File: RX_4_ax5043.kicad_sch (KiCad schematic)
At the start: 17 parts, among them U505 AX5043, U506 TPS22929D

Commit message: Add a CPU thermsistor
Signed-off-by: Corey Minyard <corey@minyard.net>
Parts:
- C550: footprint Capacitor_SMD:C_0402_1005Metric -> Capacitor_SMD:C_0603_1608Metric_Pad1.08x0.95mm_HandSolder
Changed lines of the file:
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@@
 			)
 		)
-		(property "Footprint" "Capacitor_SMD:C_0402_1005Metric"
+		(property "Footprint" "Capacitor_SMD:C_0603_1608Metric_Pad1.08x0.95mm_HandSolder"
 			(at 300.6852 85.09 0)
 			(effects

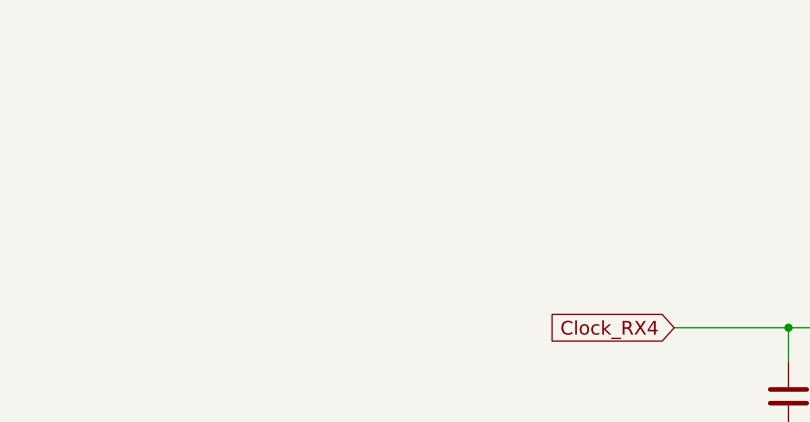
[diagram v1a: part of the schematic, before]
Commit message: Add shields around AX5043s, replace UFL connectors
Signed-off-by: Corey Minyard <corey@minyard.net>
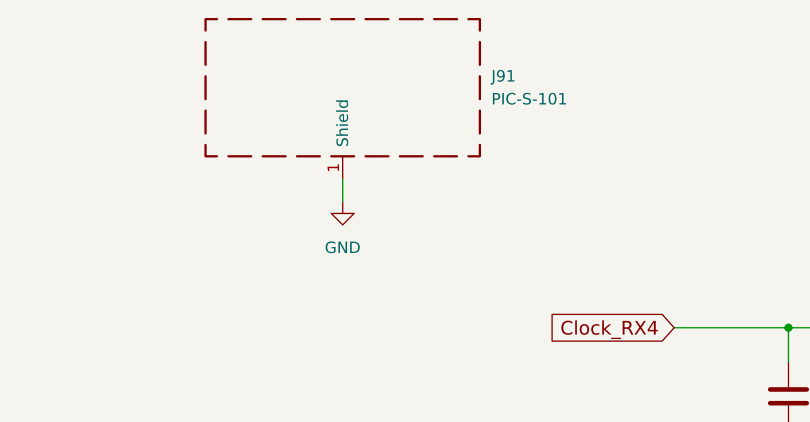
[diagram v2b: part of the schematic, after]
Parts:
- added J91: PIC-S-101, PacSatDev_misc:RF_SHIELD_PIC_S_101, symbol Device:RFShield_OnePiece
- P501: value ~ -> CONUFL001-SMD-T; footprint PacSatDev_misc:U_FL -> PacSatDev_misc:CONN1_CONUFL_TEC
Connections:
- net GND: now also J91.1 (Shield)
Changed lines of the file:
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@@
+	(wire
+		(pts
+			(xy 140.97 62.23) (xy 140.97 64.77)
+		)
+		(stroke
+			(width 0)
+			(type default)
+		)
+	)
 	(wire
 		(pts
@@
 	)
 	(symbol
+		(lib_id "Device:RFShield_OnePiece")
+		(at 140.97 52.07 0)
+		(unit 1)
+		(exclude_from_sim no)
+		(in_bom yes)
+		(on_board yes)
+		(dnp no)
+		(fields_autoplaced yes)
+		(property "Reference" "J91"
+			(at 157.48 50.7999 0)
+			(effects
+				(font
+					(size 1.27 1.27)
+				)
+				(justify left)
+			)
+		)
+		(property "Value" "PIC-S-101"
+			(at 157.48 53.3399 0)
+			(effects
+				(font
+					(size 1.27 1.27)
+				)
+				(justify left)
+			)
+		)
+		(property "Footprint" "PacSatDev_misc:RF_SHIELD_PIC_S_101"
+			(at 140.97 54.61 0)
+			(effects
+				(font
+					(size 1.27 1.27)
+				)
+				(hide yes)
+			)
+		)
+		(property "Datasheet" "~"
+			(at 140.97 54.61 0)
+			(effects
+				(font
+					(size 1.27 1.27)
+				)
+				(hide yes)
+			)
+		)
+		(property "Description" "One-piece EMI RF shielding cabinet"
+			(at 140.97 52.07 0)
+			(effects
+				(font
+					(size 1.27 1.27)
+				)
+				(hide yes)
+			)
+		)
+		(pin "1"
+		)
+		(instances
+			(project "PacSat_AFSK"
+				(path "/cc9f42d2-6985-41ac-acab-5ab7b01c5b38/f99c6a69-4136-42a1-b9ff-80c66d5e136e"
+					(reference "J91")
+					(unit 1)
+				)
+			)
+		)
+	)
+	(symbol
 		(lib_id "power:GND")
 		(at 125.73 138.43 0)
@@
 			)
 		)
-		(property "Value" "~"
+		(property "Value" "CONUFL001-SMD-T"
 			(at 109.22 125.73 0)
 			(effects
@@
 					(size 1.27 1.27)
 				)
-			)
-		)
-		(property "Footprint" "PacSatDev_misc:U_FL"
+				(hide yes)
+			)
+		)
+		(property "Footprint" "PacSatDev_misc:CONN1_CONUFL_TEC"
 			(at 109.22 125.73 0)
 			(effects
@@
 					(unit 1)
 				)
+			)
+		)
+	)
+	(symbol
+		(lib_id "power:GND")
+		(at 140.97 64.77 0)
+		(unit 1)
+		(exclude_from_sim no)
+		(in_bom yes)
+		(on_board yes)
+		(dnp no)
+		(fields_autoplaced yes)
+		(property "Reference" "#PWR0201"
+			(at 140.97 71.12 0)
+			(effects
+				(font
+					(size 1.27 1.27)
+				)
+				(hide yes)
+			)
+		)
+		(property "Value" "GND"
+			(at 140.97 69.85 0)
+			(effects
+				(font
+					(size 1.27 1.27)
+				)
+			)
+		)
+		(property "Footprint" ""
+			(at 140.97 64.77 0)
+			(effects
+				(font
+					(size 1.27 1.27)
+				)
+				(hide yes)
+			)
+		)
+		(property "Datasheet" ""
+			(at 140.97 64.77 0)
+			(effects
+				(font
+					(size 1.27 1.27)
+				)
+				(hide yes)
+			)
+		)
+		(property "Description" ""
+			(at 140.97 64.77 0)
+			(effects
+				(font
+					(size 1.27 1.27)
+				)
+			)
+		)
+		(pin "1"
+		)
+		(instances
+			(project "PacSat_AFSK"
+				(path "/cc9f42d2-6985-41ac-acab-5ab7b01c5b38/f99c6a69-4136-42a1-b9ff-80c66d5e136e"
+					(reference "#PWR0201")
+					(unit 1)
+				)

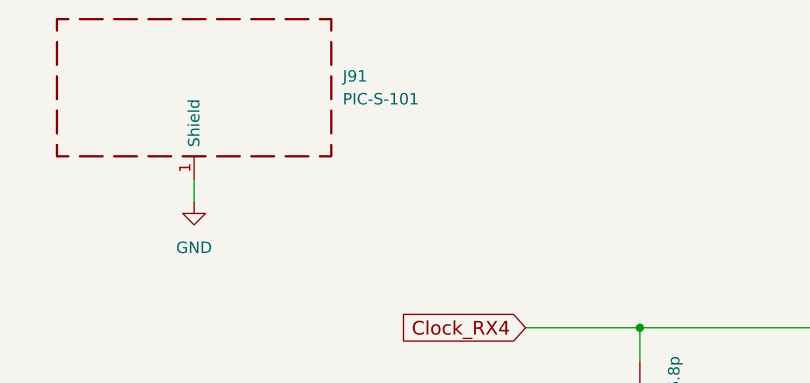
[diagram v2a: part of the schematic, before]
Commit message: More messing with RF shields
Signed-off-by: Corey Minyard <corey@minyard.net>
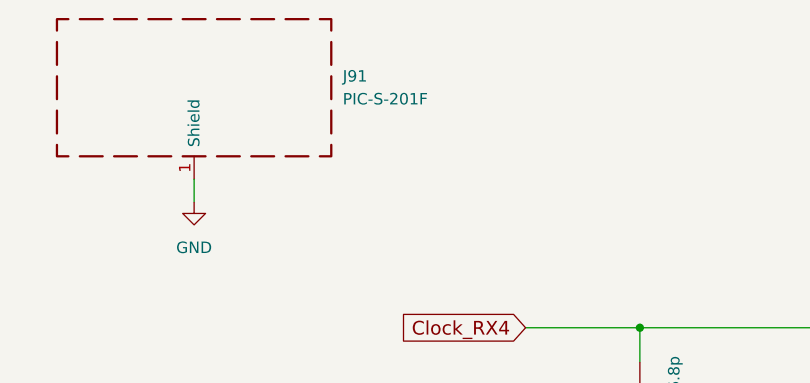
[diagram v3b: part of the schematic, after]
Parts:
- J91: value PIC-S-101 -> PIC-S-201F
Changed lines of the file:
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@@
 			)
 		)
-		(property "Value" "PIC-S-101"
+		(property "Value" "PIC-S-201F"
 			(at 157.48 53.3399 0)
 			(effects

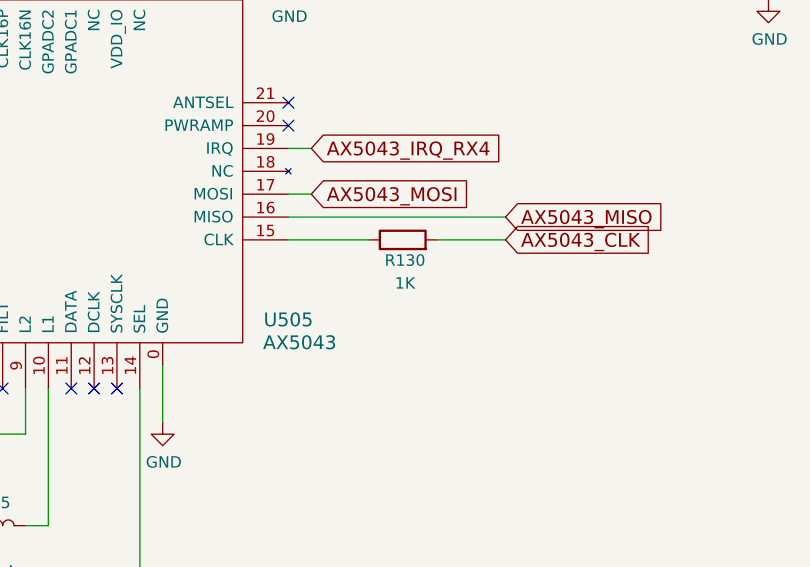
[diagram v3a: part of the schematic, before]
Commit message: Update SPI clock with simulation
Simulated the SPI clocks, updated resistor values based on findings.

Signed-off-by: Corey Minyard <corey@minyard.net>
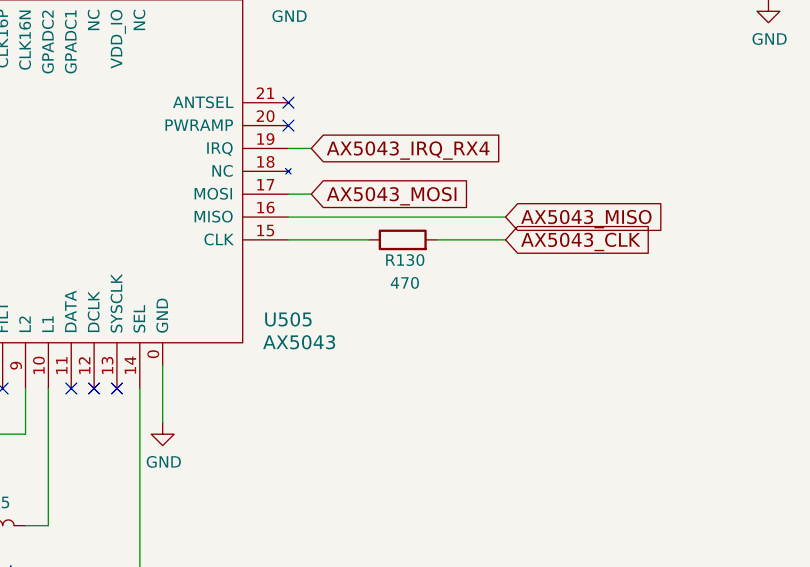
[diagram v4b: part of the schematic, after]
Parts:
- R130: value 1K -> 470
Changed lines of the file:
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@@
 			)
 		)
-		(property "Value" "1K"
+		(property "Value" "470"
 			(at 254.254 144.526 90)
 			(effects

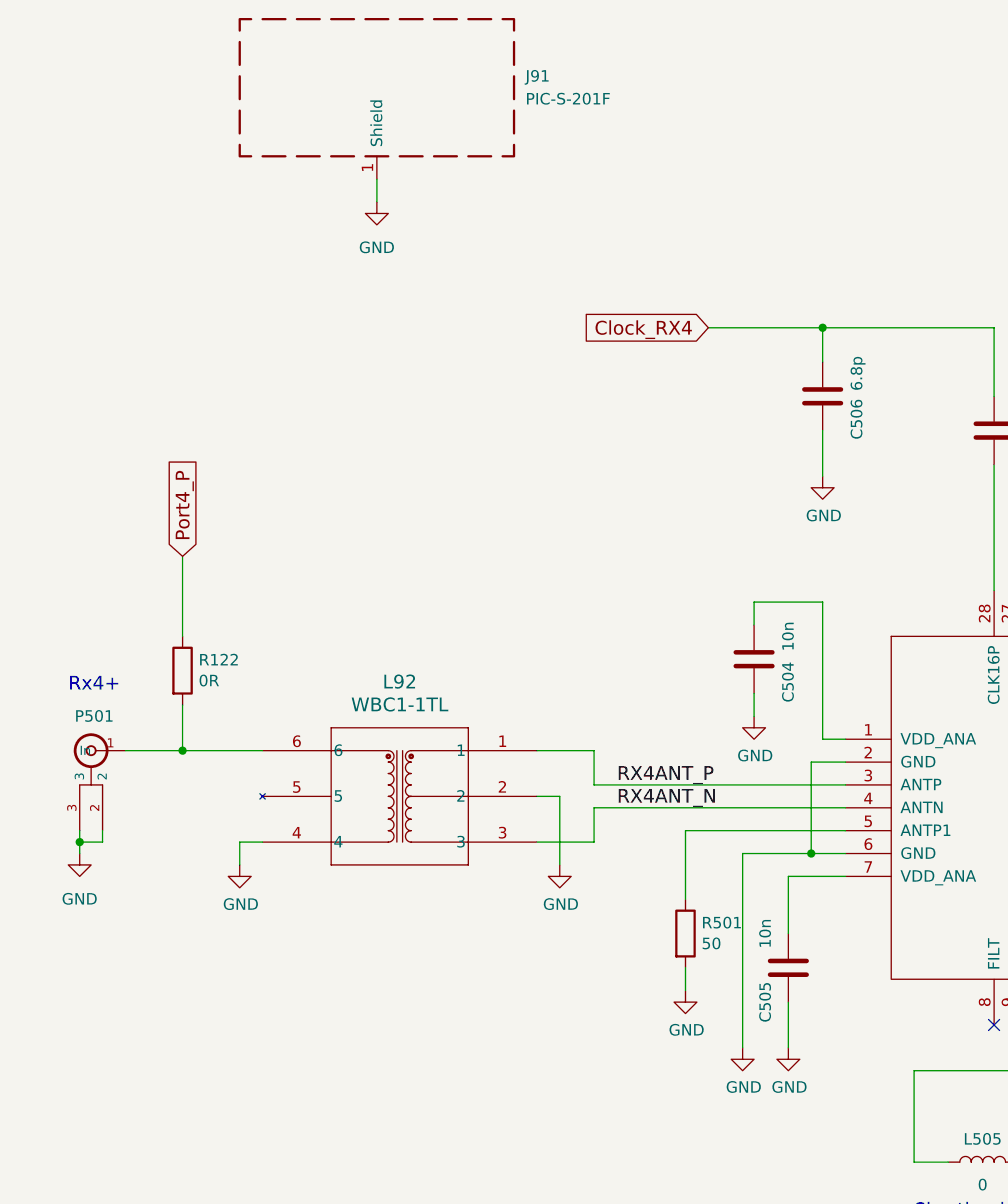
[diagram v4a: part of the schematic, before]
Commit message: Rework the AX5043 RX side to a different balun
It's cheaper (though not smaller) and fits inside the shield.

Signed-off-by: Corey Minyard <corey@minyard.net>
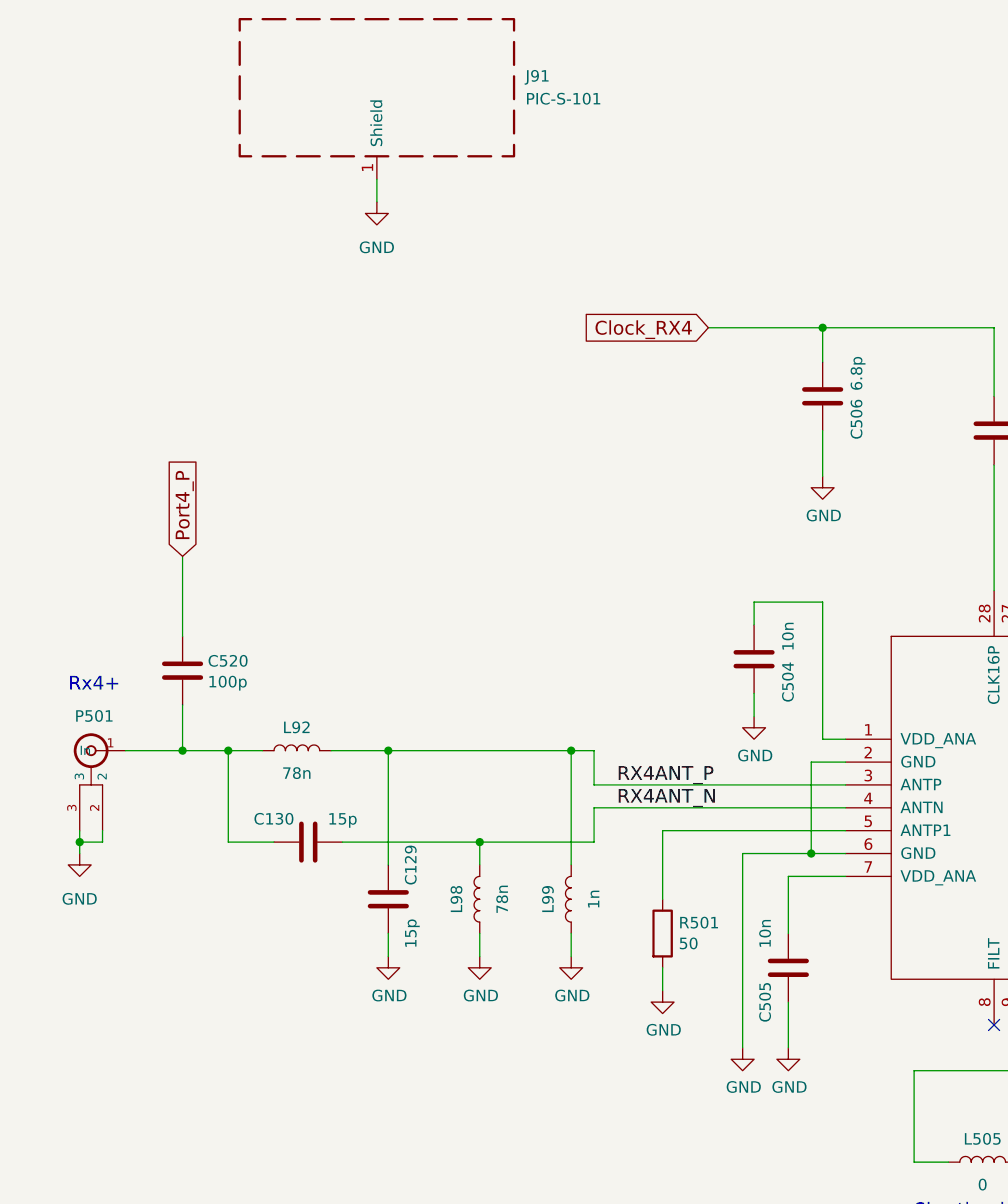
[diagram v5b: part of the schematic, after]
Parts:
- removed L92: WBC1-1TL, PacSatDev_misc:IND6_WBC1, symbol PACSAT_DEV_misc:WBC1-1TL
- added C129, C130: 15p, Capacitor_SMD:C_0603_1608Metric_Pad1.08x0.95mm_HandSolder, symbol Device:C
- added L92, L98: 78n, Inductor_SMD:L_0603_1608Metric_Pad1.05x0.95mm_HandSolder, symbol Device:L
- added L99: 1n, Inductor_SMD:L_0603_1608Metric_Pad1.05x0.95mm_HandSolder, symbol Device:L
- C520: renamed from R122; value 0R -> 100p; symbol Device:R -> Device:C
- J91: value PIC-S-201F -> PIC-S-101
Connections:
- net GND: now also C129.1, L98.1, L99.1
- net RX4ANT_N: now also C130.1, L98.2
- net RX4ANT_P: now also C129.2, L92.2, L99.2
- net at C520.2, P501.1 (In): now also C130.2, L92.1
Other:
- moved on the sheet: R501

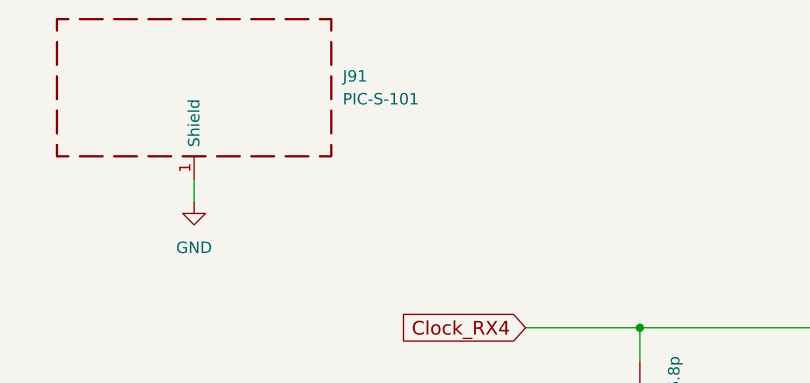
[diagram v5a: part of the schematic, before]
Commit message: Change the AX5043 shield to a frame/cover setup
Easier access to parts underneath.

Signed-off-by: Corey Minyard <corey@minyard.net>
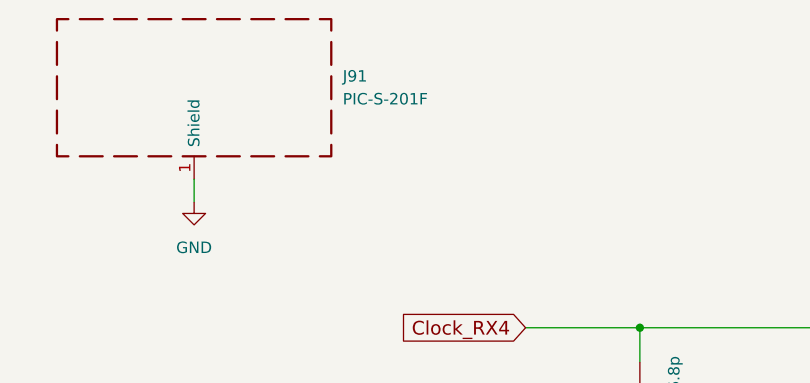
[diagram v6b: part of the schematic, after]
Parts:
- J91: value PIC-S-101 -> PIC-S-201F
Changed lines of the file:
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@@
 			)
 		)
-		(property "Value" "PIC-S-101"
+		(property "Value" "PIC-S-201F"
 			(at 157.48 53.3399 0)
 			(effects

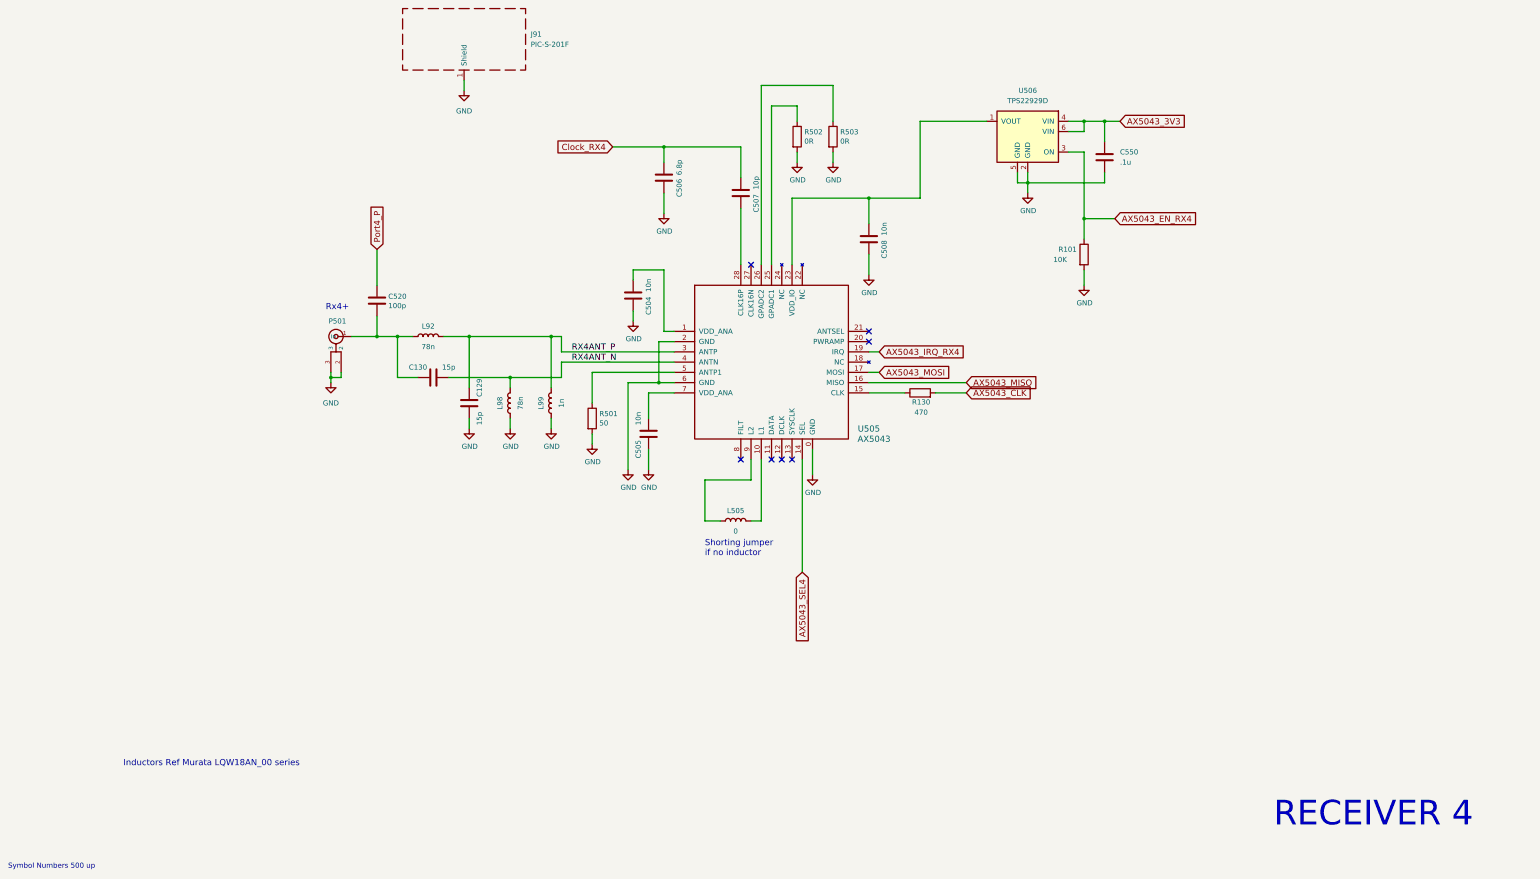
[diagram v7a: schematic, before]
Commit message: Re-annotate all parts
And get rid of the per-sheet annotation remarks.

Signed-off-by: Corey Minyard <corey@minyard.net>
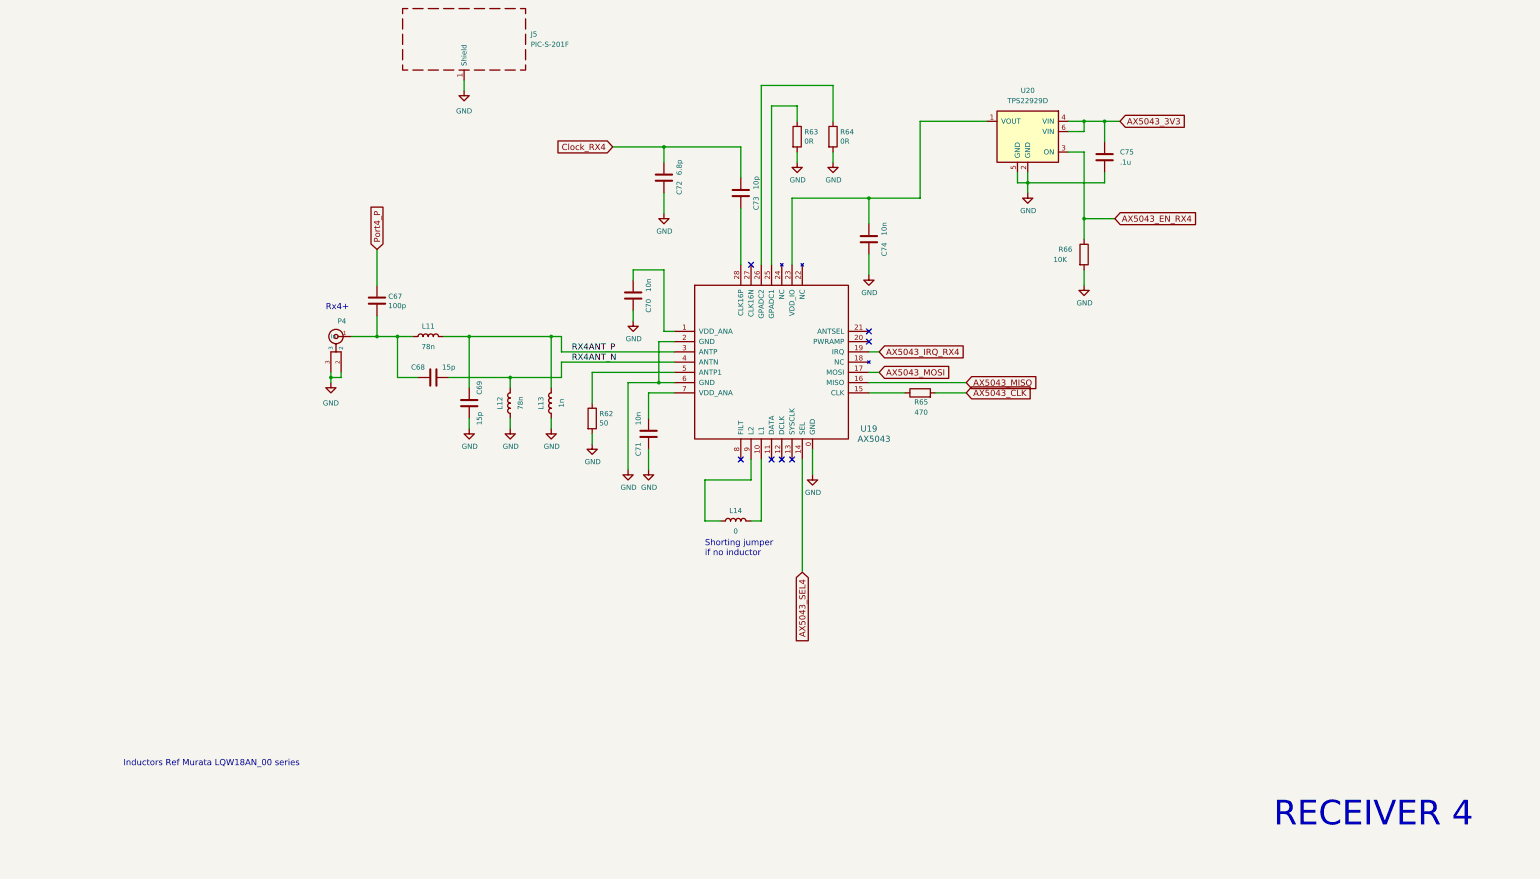
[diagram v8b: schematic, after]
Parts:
- renumbered C520 to C67, C130 to C68, C129 to C69, C504 to C70, C505 to C71, C506 to C72, C507 to C73, C508 to C74, C550 to C75, J91 to J5, L92 to L11, L98 to L12, L99 to L13, L505 to L14, P501 to P4, R501 to R62, R502 to R63, R503 to R64, R130 to R65, R101 to R66, U505 to U19, U506 to U20
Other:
- note removed: "Symbol Numbers 500 up"
